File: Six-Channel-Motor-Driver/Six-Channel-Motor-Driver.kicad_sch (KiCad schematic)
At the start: 0 parts

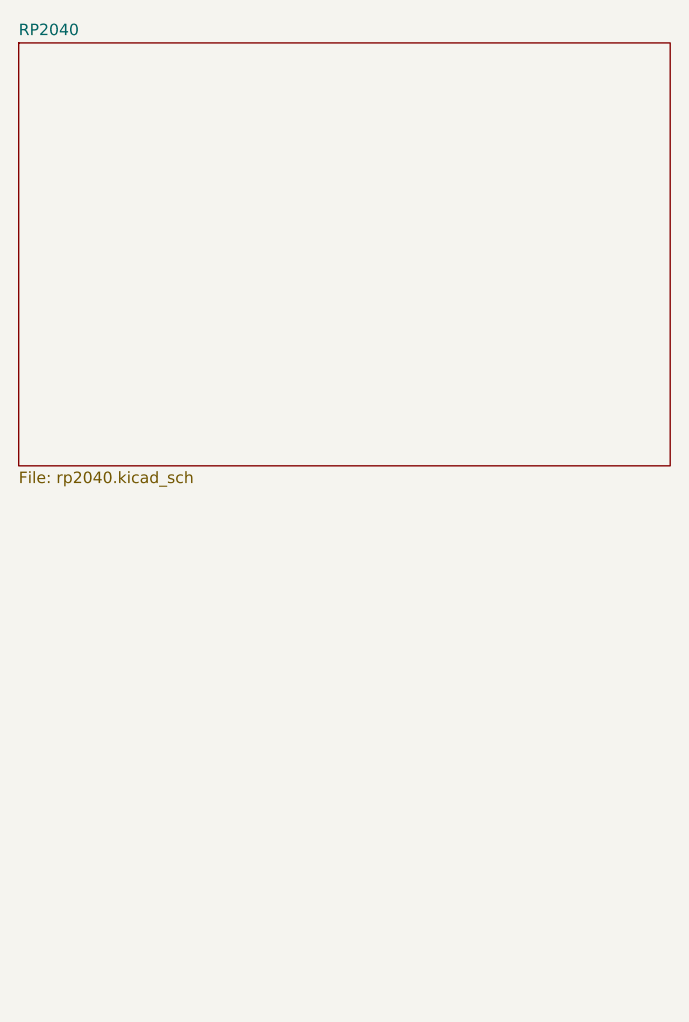
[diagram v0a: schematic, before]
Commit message: More work on MCU schematic
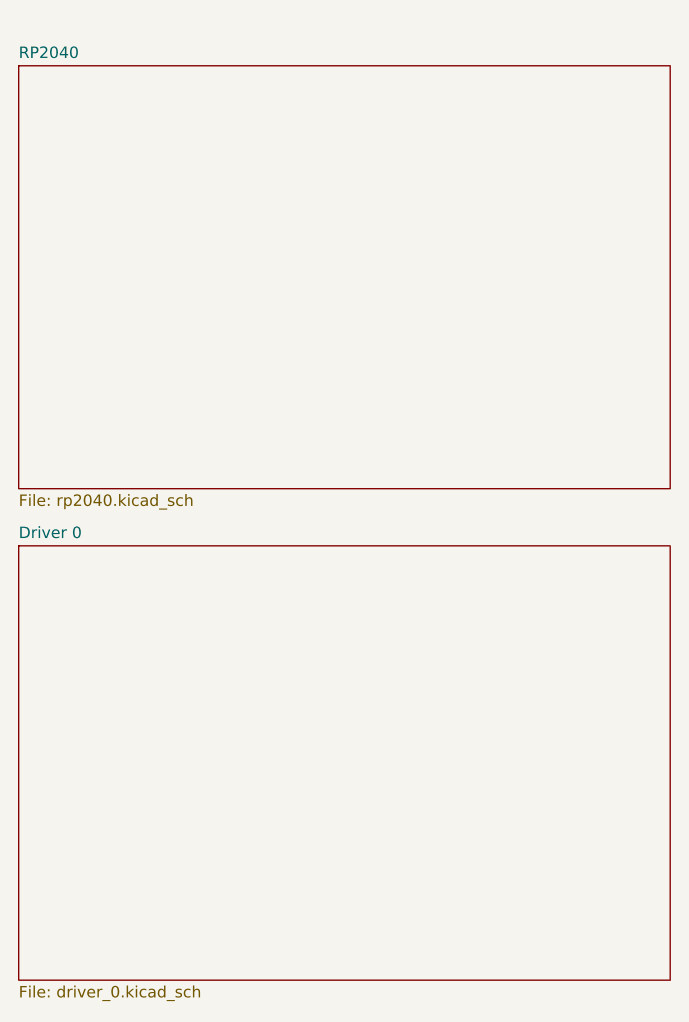
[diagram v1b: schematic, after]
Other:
- added sheet Driver 0 (driver_0.kicad_sch)

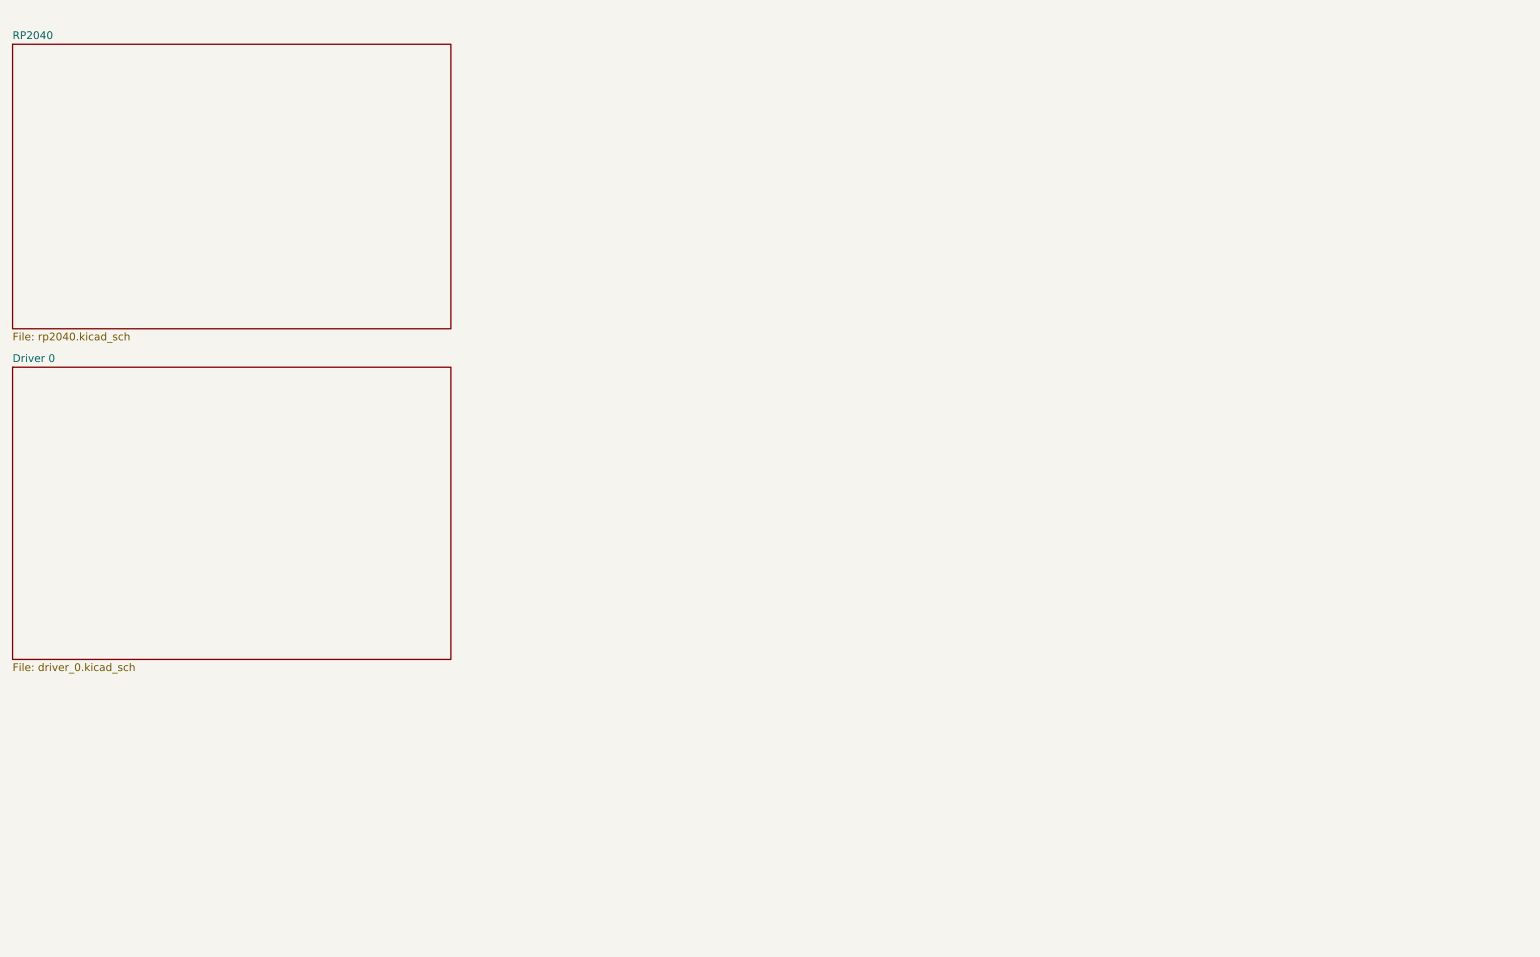
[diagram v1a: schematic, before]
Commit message: Added start of driver blocks
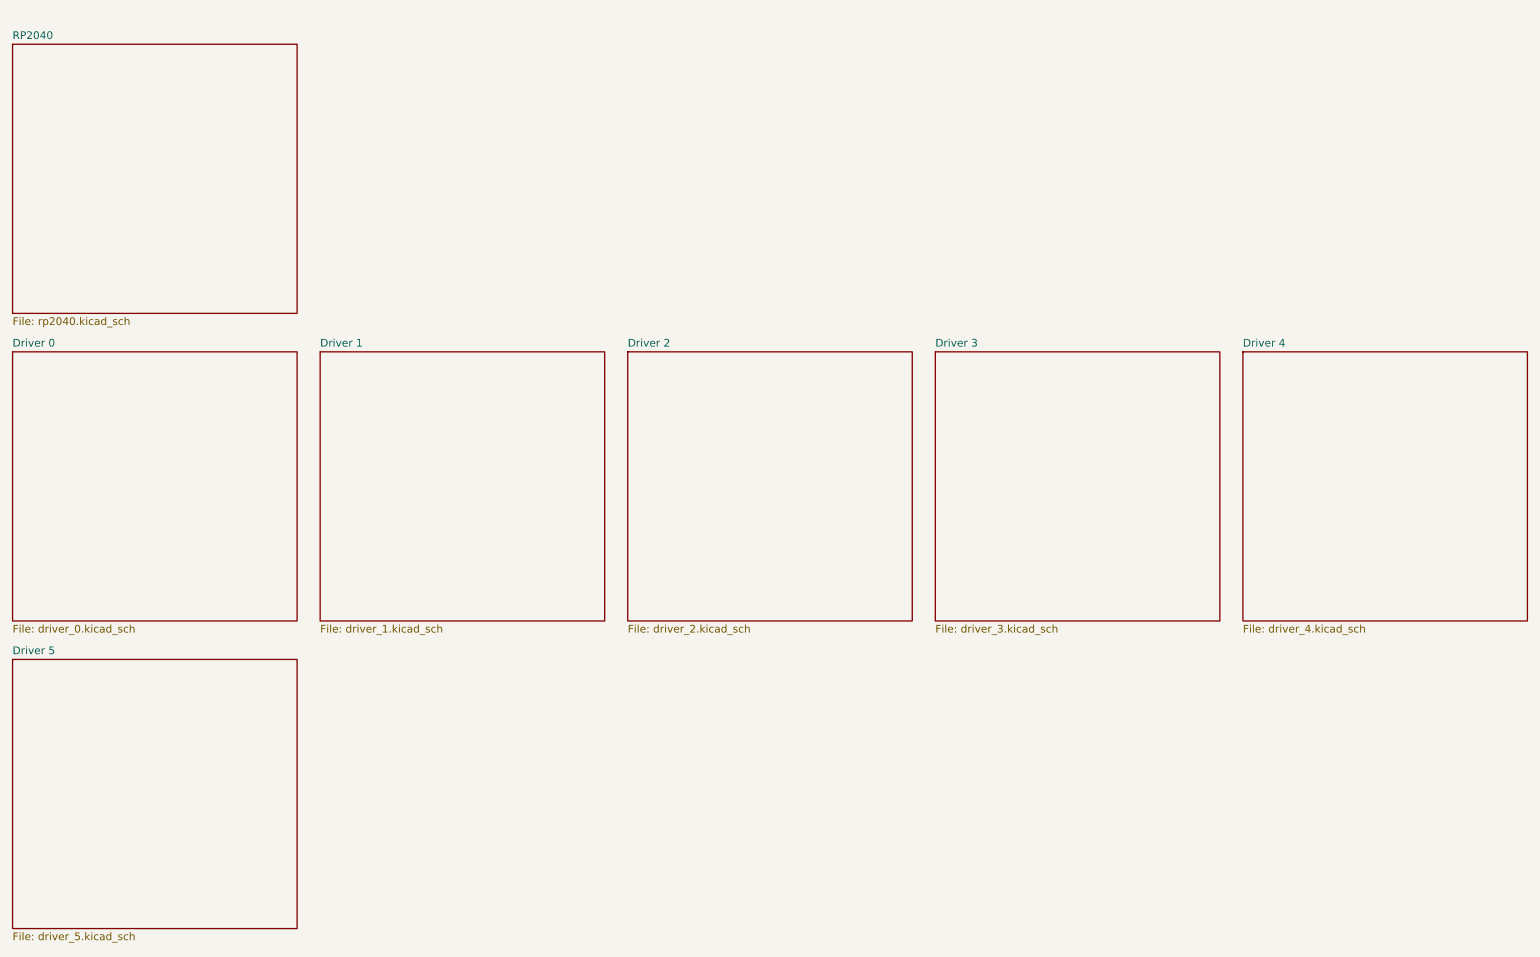
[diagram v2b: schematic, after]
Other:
- added sheet Driver 1 (driver_1.kicad_sch)
- added sheet Driver 2 (driver_2.kicad_sch)
- added sheet Driver 3 (driver_3.kicad_sch)
- added sheet Driver 4 (driver_4.kicad_sch)
- added sheet Driver 5 (driver_5.kicad_sch)
